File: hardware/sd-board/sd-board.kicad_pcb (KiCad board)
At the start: 2 copper layers, 20 x 45.5 mm, 13 parts, among them J1 TF-01A push-push, J2 FFC 6P 0.5mm, U1 74LVC1G04

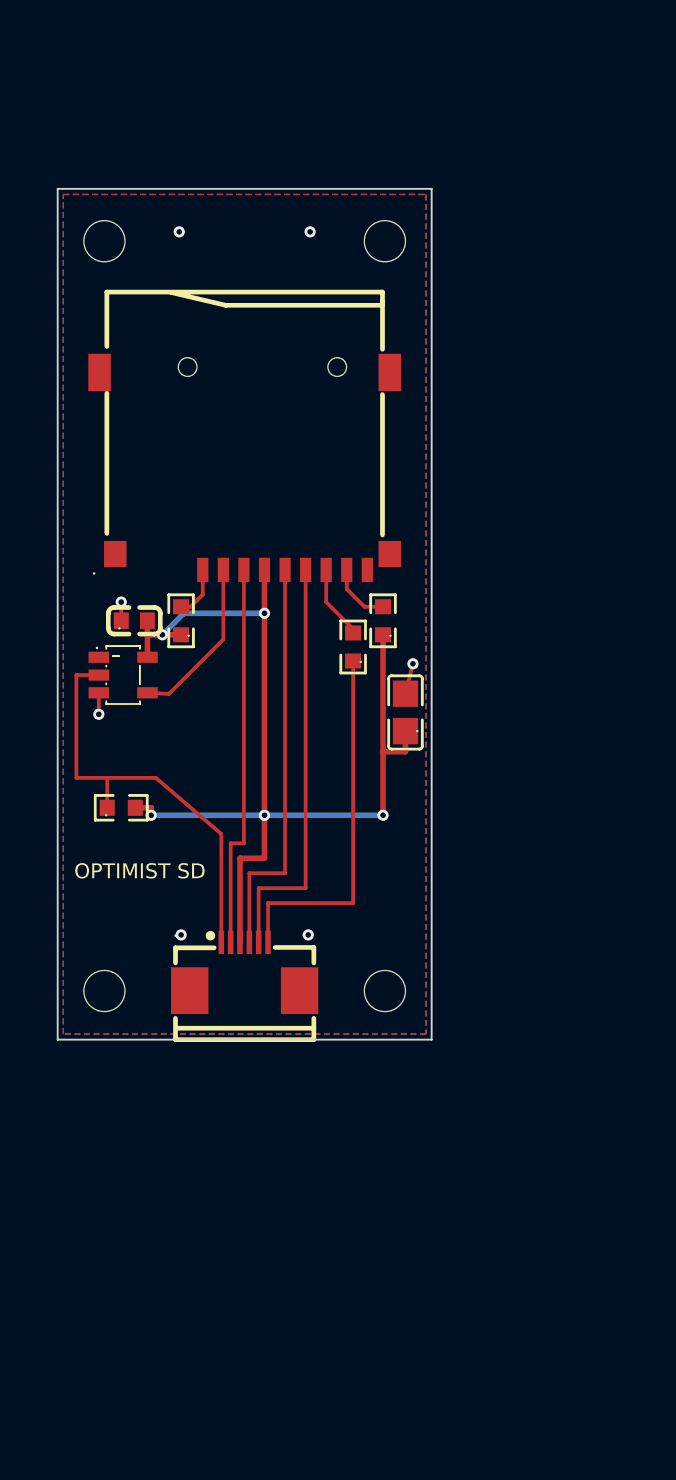
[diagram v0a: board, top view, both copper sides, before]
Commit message: feat(hardware): the SD board v3, the user's L along the left edge of the FM-1's back: a 10 mm strip from the FFC socket (where the cable comes round the board's edge) down to a 31 x 26.5 mm foot where the battery was, the card's opening on the left edge; the lines go down the strip and into the card's contacts in its own pin order (nothing crosses), 3V3 to a bus on the foot's right edge, DAT1 under the lanes; sizes read off the photo, unmeasured; DRC 0, nets 0 differ
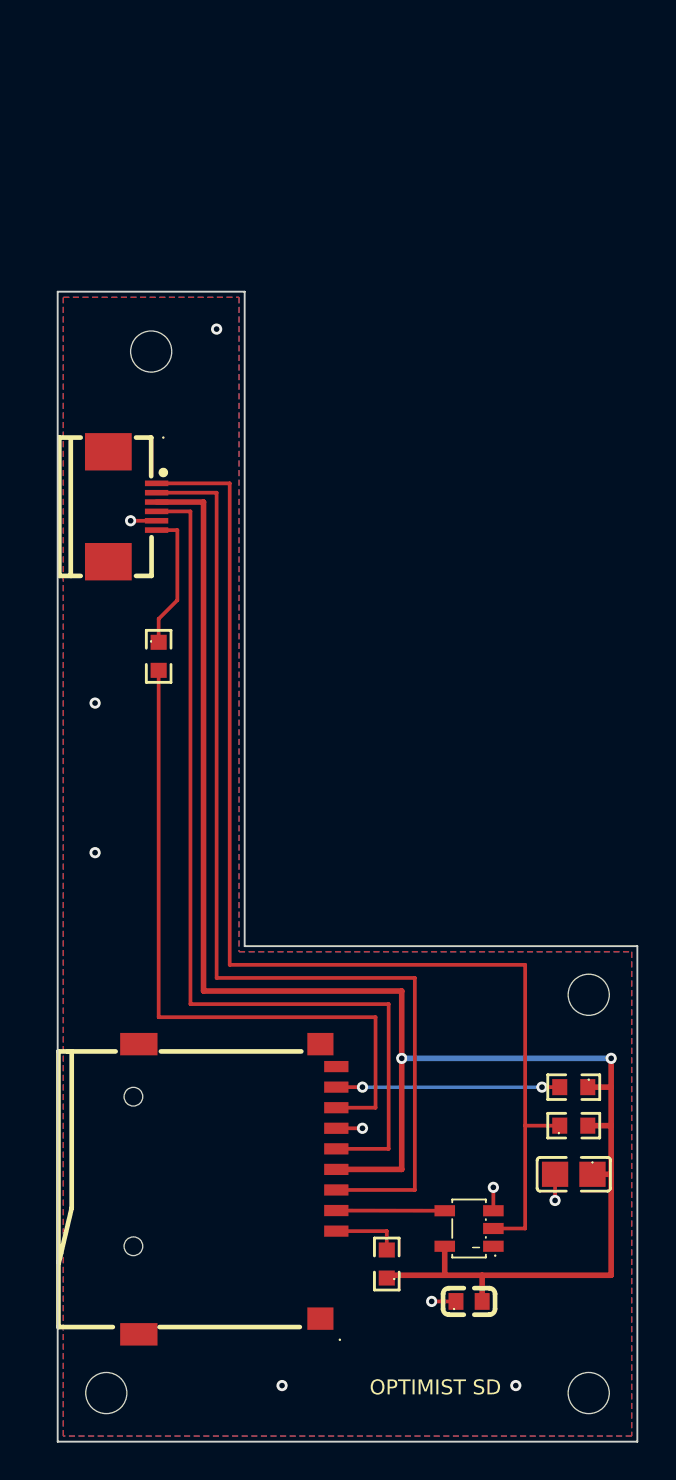
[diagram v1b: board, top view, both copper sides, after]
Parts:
- moved H2 41.7 mm to (128.4, 137.6)
- moved C2 40.6 mm to (122.0, 154.0)
- moved J1 38.4 mm to (109.6, 148.0), turned to -90 degrees
- moved R2 36.1 mm to (117.6, 152.0)
- moved U1 34.9 mm to (122.0, 150.1), turned to 0 degrees
- moved H3 33.7 mm to (128.4, 158.9)
- moved R4 29.6 mm to (127.6, 144.6)
- moved R3 26.9 mm to (127.6, 142.5), turned to 180 degrees
- moved C1 26.3 mm to (127.6, 147.2), turned to 180 degrees
- moved H4 26.2 mm to (102.6, 158.9)
- moved J2 25.3 mm to (104.0, 111.5), turned to -90 degrees
- moved R1 10.4 mm to (105.4, 119.5), turned to -90 degrees
- moved H1 6.41 mm to (105.0, 103.2)
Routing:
- net LCD_CS: track 23.0 -> 63.1 mm
- net 3V3: track 56.5 -> 93.5 mm, vias 5 -> 2
- net MOSI: track 20.6 -> 55.3 mm
- net DAT0: track 3.97 -> 37.1 mm
- net CLK: track 21.8 -> 49.3 mm
- net GND: track 26.2 -> 6.74 mm, vias 7 -> 10
- net MISO: track 19.6 -> 7.52 mm
- net DAT1: track 3.35 -> 11.9 mm, vias 0 -> 2
- net CARD_CS: track 8.99 -> 5.80 mm
- net DAT2: track 2.75 -> 3.71 mm
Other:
- board size 20 x 45.5 mm -> 31 x 61.5 mm

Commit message: feat(hardware): SD board v3 held by two of the FM-1's own screws (38.1 mm apart, measured; the case's poles 6.8 mm, measured), the inverter and its parts moved into the strip under the FFC socket so the foot is 22 mm wide, not 31 (the battery moves less); CS and 3V3 reach the card on the bottom round the lower screw; FFC order MOSI CLK MISO GND 3V3 CS; MEASUREMENTS.md (measured vs photo), a 3D-print mockup.stl and a 1:1 template; DRC 0, nets 0 differ
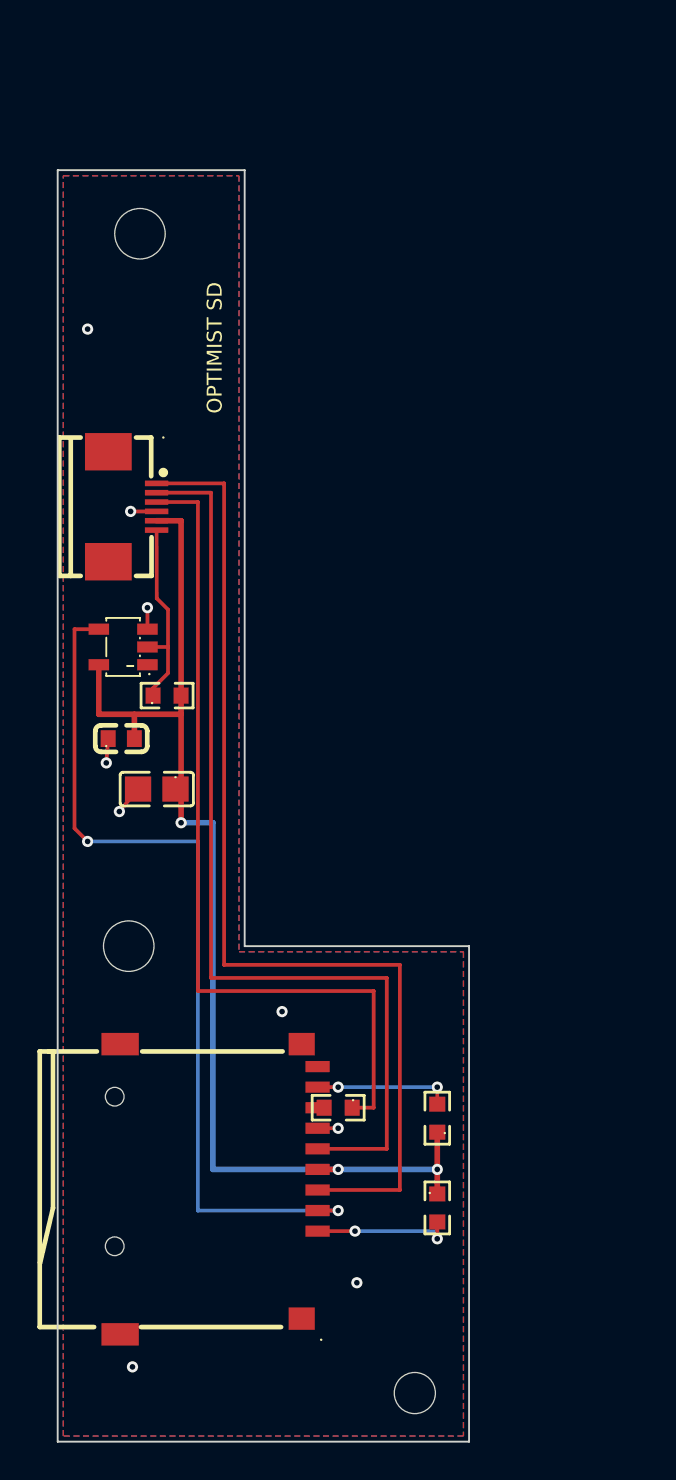
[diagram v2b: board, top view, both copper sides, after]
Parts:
- removed H4: M2, MountingHole:MountingHole_2.2mm_M2
- H1, H2: value M2 -> M2.5; footprint MountingHole:MountingHole_2.2mm_M2 -> MountingHole:MountingHole_2.7mm_M2.5
- moved H2 47.2 mm to (104.4, 96.9)
- moved U1 36.2 mm to (103.5, 119.0)
- moved C2 35.4 mm to (103.4, 123.9)
- moved H1 31.8 mm to (103.8, 135.0)
- moved R4 31.7 mm to (105.8, 121.6)
- moved C1 30.4 mm to (105.3, 126.6)
- moved R1 26.0 mm to (115.0, 143.6), turned to 180 degrees
- moved H3 9.30 mm to (119.1, 158.9)
- moved R3 7.49 mm to (120.3, 144.2), turned to 90 degrees
- moved R2 4.04 mm to (120.3, 149.0), turned to -90 degrees
- moved J1 1.00 mm to (108.6, 148.0)
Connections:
- J2 pad 1: LCD_CS -> MOSI
- J2 pad 2: MOSI -> CLK
- J2 pad 3: 3V3 -> MISO
- J2 pad 4: CLK -> GND
- J2 pad 5: GND -> 3V3
- J2 pad 6: MISO -> LCD_CS
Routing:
- net LCD_CS: track 63.1 -> 10.5 mm
- net CARD_CS: track 5.80 -> 47.2 mm, vias 0 -> 2
- net MISO: track 7.52 -> 45.1 mm
- net DAT0: track 37.1 -> 0.35 mm
- net 3V3: track 93.5 -> 62.4 mm, vias 2 -> 3
- net DAT1: track 11.9 -> 7.31 mm
- net DAT2: track 3.71 -> 7.71 mm, vias 0 -> 2
- net CLK: track 49.3 -> 51.1 mm
- net GND: track 6.74 -> 6.51 mm, vias 10 -> 9
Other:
- board size 31 x 61.5 mm -> 22 x 68 mm

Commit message: feat(hardware): SD board v3: the tie hole dropped (the two FM-1 screws hold it), the foot trimmed to the card socket (22 x 22.6 mm past the lower screw; the user's cover sketch shows the same L)
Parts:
- removed H3: M2, MountingHole:MountingHole_2.2mm_M2
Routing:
- net GND: vias 9 -> 8
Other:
- board size 22 x 68 mm -> 22 x 64.1 mm

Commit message: feat(hardware): SD board v3: the back cover's poles pass through it (the user): two 5.5 mm holes (pole 5.2 from a photo + 0.3), centres 38.1 - 5.2 apart (38.1 over the outer edges, measured); the strip's top 1.5 mm above the upper hole
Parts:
- H1, H2: value M2.5 -> pole; footprint MountingHole:MountingHole_2.7mm_M2.5 -> sdboard:PoleHole
- moved H2 5.20 mm to (104.4, 102.1)
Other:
- board size 22 x 64.1 mm -> 22 x 59.8 mm

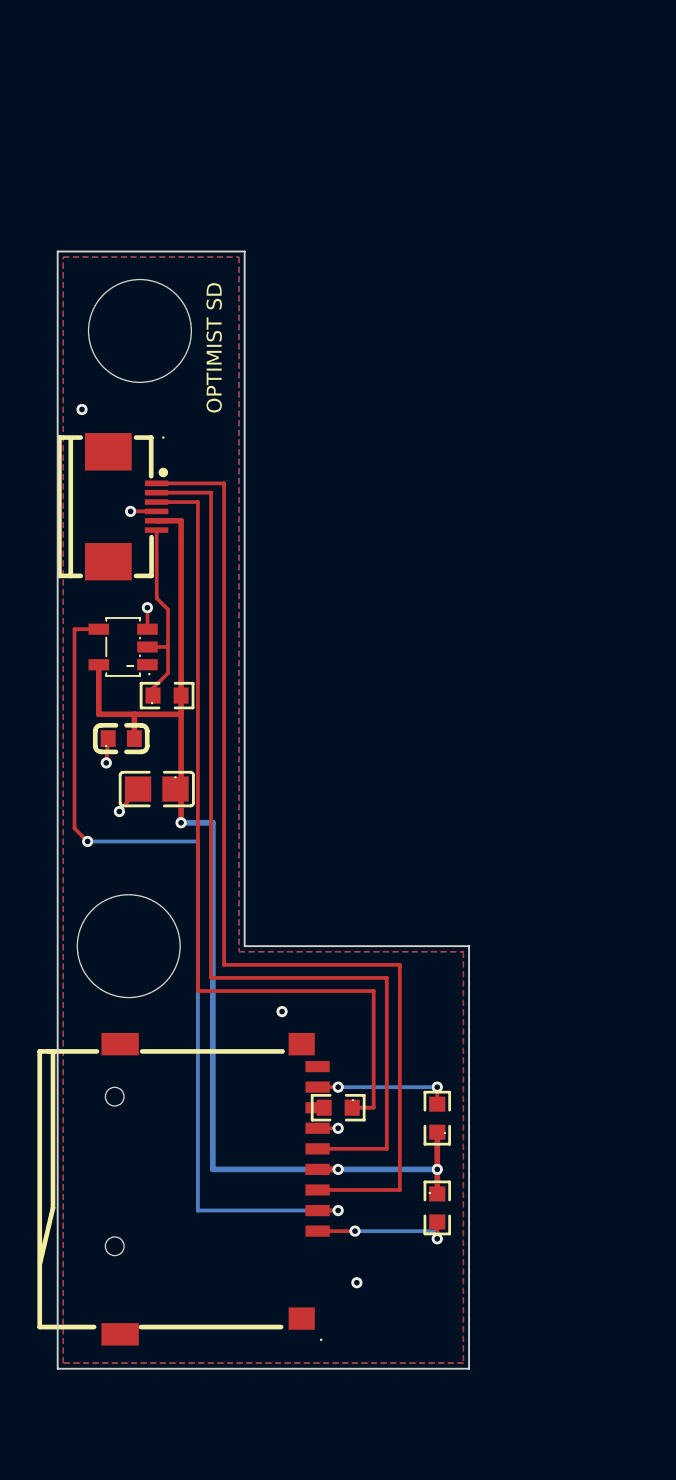
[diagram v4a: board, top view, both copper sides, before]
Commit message: feat(hardware): SD board v3 on the user's caliper measurements (MEASUREMENTS.md, a to j): the poles are 6.9 mm with their centres 3.4 mm in, so they stand over the edge: two U-notches open to the left (0.6 mm play), 45.55 mm apart (the board's 46.1 and the cover's 45 differ by 1.1); 38.1 was between the poles' facing edges; the strip's top at the FM-1 board's top edge, lanes clear of the notches; no holes left
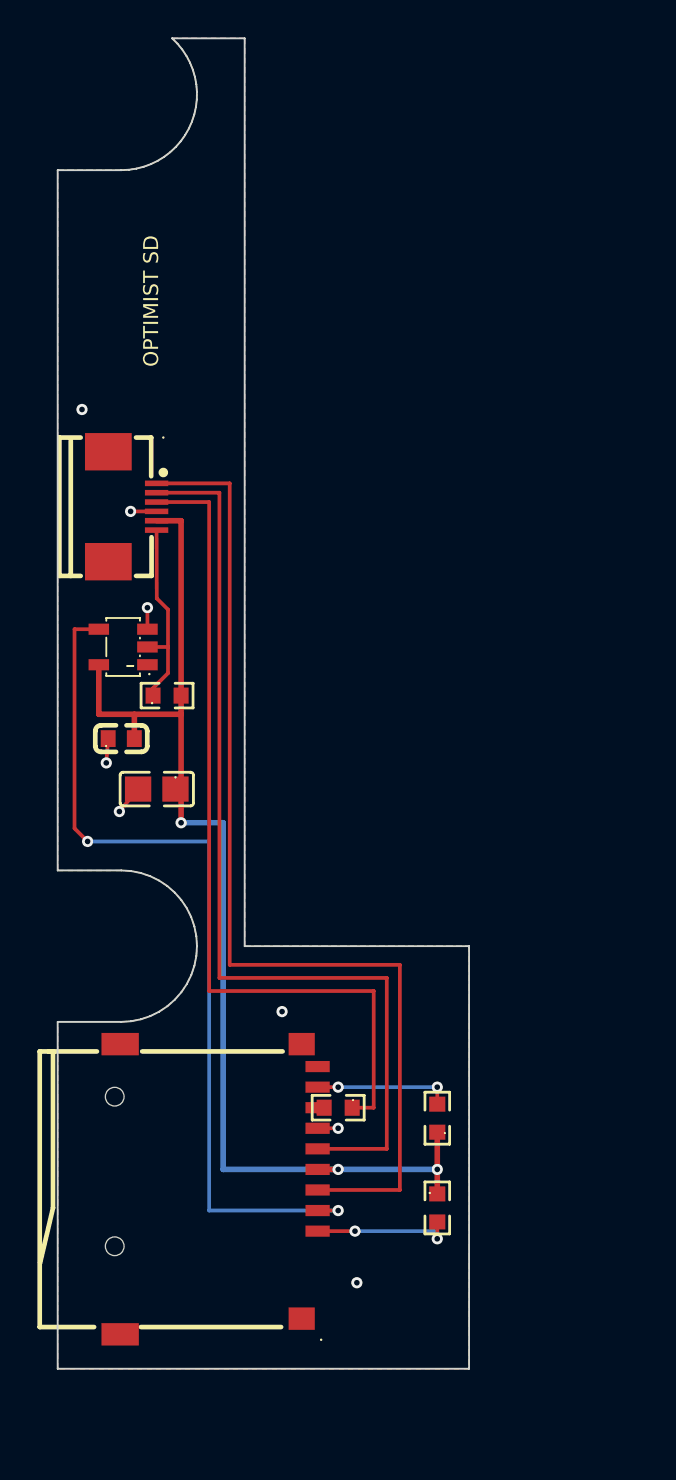
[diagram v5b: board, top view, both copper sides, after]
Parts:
- removed H1, H2: pole, sdboard:PoleHole
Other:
- board size 22 x 59.8 mm -> 22 x 71.1 mm
